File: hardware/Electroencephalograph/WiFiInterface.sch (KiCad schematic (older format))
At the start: 18 parts

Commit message: fix esp circuit
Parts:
- added R109, R110: 0R, Resistor_SMD:R_0402_1005Metric, symbol Device:R
- gave numbers to parts that had none: 18
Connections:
- net DP_GND: now also U12.9 (GND)
- net ESP_RX: now also R110.1; no longer J7.3 (Pin_3), U12.15 (RXD)
- net ESP_TX: now also R109.1; no longer J7.2 (Pin_2), U12.16 (TXD)
- net CS_ESP: now reaches U12.17 (CS0)
- net MISO: now reaches U12.18 (MISO)
- net MOSI: now reaches U12.21 (MOSI)
- net SCK: now reaches U12.22 (SCLK)
- net at U12.8 (VCC): now also C16.1, C17.1, Q2.3 (D), R103.1, R105.1, R106.1, R107.1
- new net: J7.3 (Pin_3), R110.2, U12.15 (RXD)
- new net: J7.2 (Pin_2), R109.2, U12.16 (TXD)
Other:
- moved on the sheet: D40, D41, J7, Q3, R102, R103, R104, R105, R106, R107, R108, U12

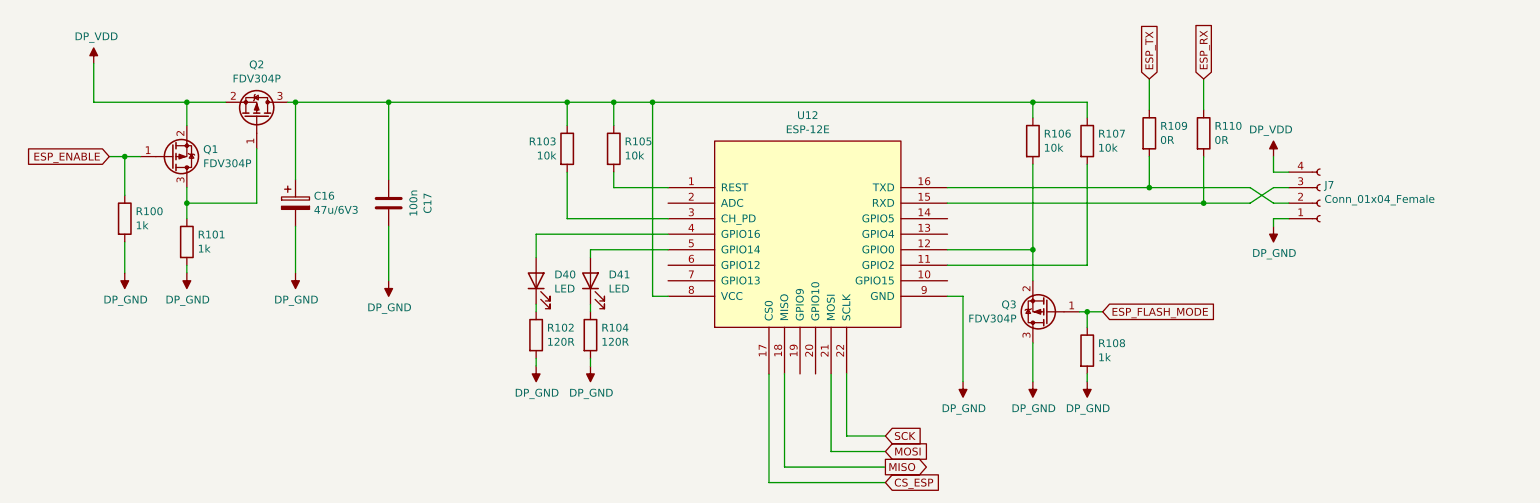
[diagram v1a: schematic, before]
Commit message: improve mcu component placement on pcb
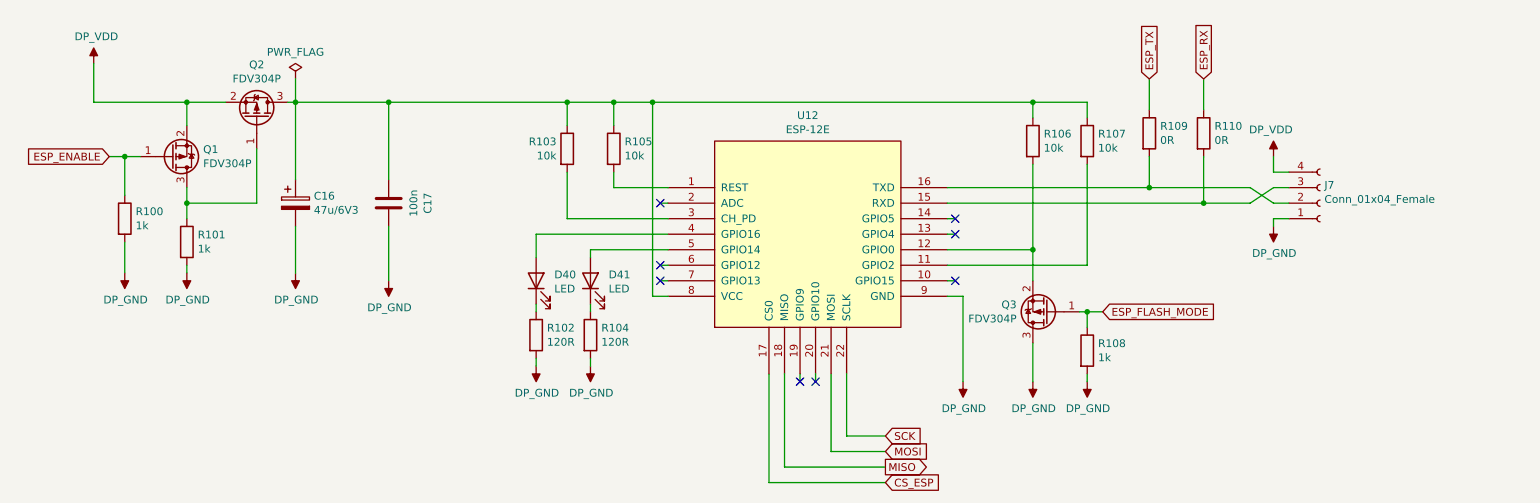
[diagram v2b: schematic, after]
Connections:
- no-connect marks 0 -> 8
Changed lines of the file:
@@
 Wire Wire Line
 	6200 5150 6200 4450
+Wire Wire Line
+	7350 3450 7400 3450
+Wire Wire Line
+	7350 3550 7400 3550
+Wire Wire Line
+	7350 3850 7400 3850
+NoConn ~ 7400 3450
+NoConn ~ 7400 3550
+NoConn ~ 7400 3850
+Wire Wire Line
+	5550 3350 5500 3350
+Wire Wire Line
+	5550 3750 5500 3750
+Wire Wire Line
+	5550 3850 5500 3850
+NoConn ~ 5500 3350
+NoConn ~ 5500 3750
+NoConn ~ 5500 3850
+Wire Wire Line
+	6400 4450 6400 4500
+Wire Wire Line
+	6500 4450 6500 4500
+NoConn ~ 6500 4500
+NoConn ~ 6400 4500
+$Comp
+L power:PWR_FLAG #FLG03
+U 1 1 5F0EAABE
+P 3150 2550
+F 0 "#FLG03" H 3150 2625 50  0001 C CNN
+F 1 "PWR_FLAG" H 3150 2723 50  0000 C CNN
+F 2 "" H 3150 2550 50  0001 C CNN
+F 3 "~" H 3150 2550 50  0001 C CNN
+	1    3150 2550
+	1    0    0    -1
+$EndComp
+Wire Wire Line
+	3150 2550 3150 2700
 $EndSCHEMATC

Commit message: draft of mcu routing
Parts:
- removed Q3: FDV304P, Package_TO_SOT_SMD:SOT-23, symbol Device:Q_PMOS_GSD
- removed R106: 10k, Resistor_SMD:R_0402_1005Metric, symbol Device:R
- added R116, R117: 0R, Resistor_SMD:R_0402_1005Metric, symbol Device:R
- R108: value 1k -> 10k
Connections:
- net DP_GND: no longer R108.2
- net ESP_FLASH_MODE: now also R108.2, U12.12 (GPIO0); no longer R108.1
- net at R110.2, U12.15 (RXD): now also R117.2; no longer J7.3 (Pin_3)
- net at R109.2, U12.16 (TXD): now also R116.2; no longer J7.2 (Pin_2)
- net at C16.1, C17.1, Q2.3 (D)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: now also R108.1
- new net: J7.2 (Pin_2), R116.1
- new net: J7.3 (Pin_3), R117.1
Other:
- moved on the sheet: C16, C17, Q1, Q2, R100, R101, R105, R107, R108, R109, R110

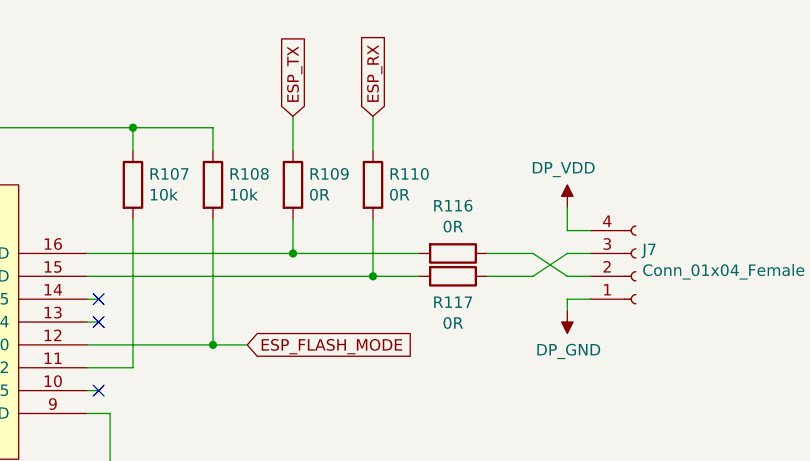
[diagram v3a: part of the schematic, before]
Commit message: further routing of cpu part
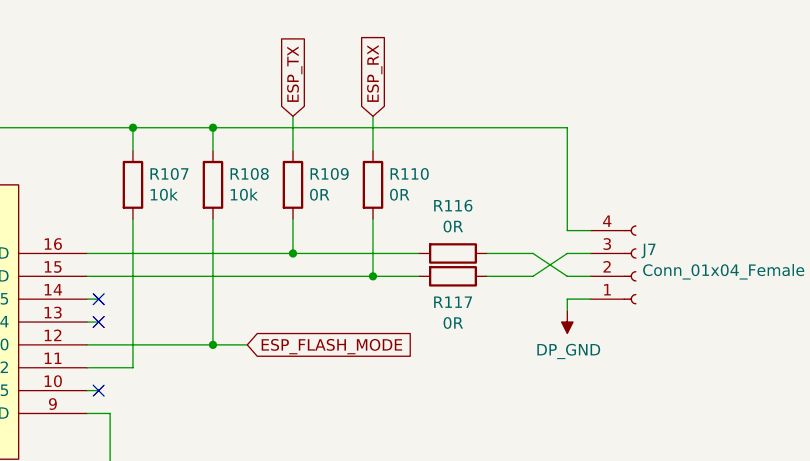
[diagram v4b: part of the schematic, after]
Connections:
- net DP_VDD: no longer J7.4 (Pin_4)
- net at C16.1, C17.1, Q2.3 (D)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: now also J7.4 (Pin_4)
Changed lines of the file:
@@
 	9550 3150 9450 3150
 Wire Wire Line
-	9450 3150 9450 3050
-Wire Wire Line
 	9450 3450 9450 3500
 Wire Wire Line
 	9550 3450 9450 3450
-$Comp
-L Electroencephalograph:DP_VDD #PWR?
-U 1 1 5F02CA0E
-P 9450 3050
-AR Path="/5E142744/5F02CA0E" Ref="#PWR?"  Part="1"
-AR Path="/5E27E78E/5F02CA0E" Ref="#PWR?"  Part="1"
-AR Path="/5F01FBEA/5F02CA0E" Ref="#PWR230"  Part="1"
-F 0 "#PWR230" H 9450 3175 50  0001 C CNN
-F 1 "DP_VDD" H 9467 3223 50  0000 C CNN
-F 2 "" H 9450 3175 50  0001 C CNN
-F 3 "" H 9450 3175 50  0001 C CNN
-	1    9450 3050
-	-1   0    0    -1
-$EndComp
 Wire Wire Line
 	4900 2700 4900 2850
@@
 Wire Wire Line
 	7900 3650 8050 3650
+Wire Wire Line
+	7900 2700 9450 2700
+Wire Wire Line
+	9450 2700 9450 3150
+Connection ~ 7900 2700
 $EndSCHEMATC

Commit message: further routing of mcu part
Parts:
- added C18: 100n, Capacitor_SMD:C_0402_1005Metric, symbol Device:C
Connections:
- net DP_GND: now also C18.2
- net at C16.1, C17.1, J7.4 (Pin_4)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: now also C18.1
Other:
- moved on the sheet: J7, R108, R109, R110, R116, R117
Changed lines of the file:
@@
 L Connector:Conn_01x04_Female J?
 U 1 1 5F02C9FE
-P 9750 3350
+P 10200 3350
 AR Path="/5E142744/5F02C9FE" Ref="J?"  Part="1"
 AR Path="/5E27E78E/5F02C9FE" Ref="J?"  Part="1"
 AR Path="/5F01FBEA/5F02C9FE" Ref="J7"  Part="1"
-F 0 "J7" H 9778 3234 50  0000 L CNN
-F 1 "Conn_01x04_Female" H 9778 3325 50  0000 L CNN
-F 2 "Connector_PinHeader_2.54mm:PinHeader_1x04_P2.54mm_Vertical" H 9750 3350 50  0001 C CNN
-F 3 "~" H 9750 3350 50  0001 C CNN
-	1    9750 3350
+F 0 "J7" H 10228 3234 50  0000 L CNN
+F 1 "Conn_01x04_Female" H 10228 3325 50  0000 L CNN
+F 2 "Connector_PinHeader_2.54mm:PinHeader_1x04_P2.54mm_Vertical" H 10200 3350 50  0001 C CNN
+F 3 "~" H 10200 3350 50  0001 C CNN
+	1    10200 3350
 	1    0    0    1
 $EndComp
@@
 L Electroencephalograph:DP_GND #PWR?
 U 1 1 5F02CA04
-P 9450 3500
+P 9900 3500
 AR Path="/5F02CA04" Ref="#PWR?"  Part="1"
 AR Path="/5DAEEEF4/5F02CA04" Ref="#PWR?"  Part="1"
@@
 AR Path="/5E27E78E/5F02CA04" Ref="#PWR?"  Part="1"
 AR Path="/5F01FBEA/5F02CA04" Ref="#PWR231"  Part="1"
-F 0 "#PWR231" H 9450 3250 50  0001 C CNN
-F 1 "DP_GND" H 9455 3327 50  0000 C CNN
-F 2 "" H 9450 3500 50  0001 C CNN
-F 3 "" H 9450 3500 50  0001 C CNN
-	1    9450 3500
-	1    0    0    -1
-$EndComp
-Wire Wire Line
-	9550 3150 9450 3150
-Wire Wire Line
-	9450 3450 9450 3500
-Wire Wire Line
-	9550 3450 9450 3450
+F 0 "#PWR231" H 9900 3250 50  0001 C CNN
+F 1 "DP_GND" H 9905 3327 50  0000 C CNN
+F 2 "" H 9900 3500 50  0001 C CNN
+F 3 "" H 9900 3500 50  0001 C CNN
+	1    9900 3500
+	1    0    0    -1
+$EndComp
+Wire Wire Line
+	10000 3150 9900 3150
+Wire Wire Line
+	9900 3450 9900 3500
+Wire Wire Line
+	10000 3450 9900 3450
 Wire Wire Line
 	4900 2700 4900 2850
@@
 L Device:R R?
 U 1 1 5F02CA80
-P 7900 2950
+P 8350 2950
 AR Path="/5DD5C7F6/5F02CA80" Ref="R?"  Part="1"
 AR Path="/5DD5CD1D/5F02CA80" Ref="R?"  Part="1"
 AR Path="/5E27E78E/5F02CA80" Ref="R?"  Part="1"
 AR Path="/5F01FBEA/5F02CA80" Ref="R108"  Part="1"
-F 0 "R108" H 7970 2996 50  0000 L CNN
-F 1 "10k" H 7970 2905 50  0000 L CNN
-F 2 "Resistor_SMD:R_0402_1005Metric" V 7830 2950 50  0001 C CNN
-F 3 "~" H 7900 2950 50  0001 C CNN
-	1    7900 2950
-	1    0    0    -1
-$EndComp
-Text GLabel 8050 3650 2    50   Input ~ 0
+F 0 "R108" H 8420 2996 50  0000 L CNN
+F 1 "10k" H 8420 2905 50  0000 L CNN
+F 2 "Resistor_SMD:R_0402_1005Metric" V 8280 2950 50  0001 C CNN
+F 3 "~" H 8350 2950 50  0001 C CNN
+	1    8350 2950
+	1    0    0    -1
+$EndComp
+Text GLabel 8500 3650 2    50   Input ~ 0
 ESP_FLASH_MODE
 Wire Wire Line
-	9300 3350 9450 3250
-Wire Wire Line
-	9450 3350 9300 3250
-Wire Wire Line
-	9450 3250 9550 3250
-Wire Wire Line
-	9450 3350 9550 3350
-Wire Wire Line
-	8600 3350 8600 3100
-Wire Wire Line
-	8600 3350 8800 3350
-Text GLabel 8250 2650 1    50   Input ~ 0
+	9750 3350 9900 3250
+Wire Wire Line
+	9900 3350 9750 3250
+Wire Wire Line
+	9900 3250 10000 3250
+Wire Wire Line
+	9900 3350 10000 3350
+Wire Wire Line
+	9050 3350 9050 3100
+Wire Wire Line
+	9050 3350 9250 3350
+Text GLabel 8700 2650 1    50   Input ~ 0
 ESP_TX
-Text GLabel 8600 2650 1    50   Input ~ 0
+Text GLabel 9050 2650 1    50   Input ~ 0
 ESP_RX
 Wire Wire Line
-	7350 3350 8600 3350
-Connection ~ 8600 3350
+	7350 3350 9050 3350
+Connection ~ 9050 3350
 $Comp
 L Device:LED D?
@@
 L Device:R R?
 U 1 1 5F04FD04
-P 8250 2950
+P 8700 2950
 AR Path="/5DD5C7F6/5F04FD04" Ref="R?"  Part="1"
 AR Path="/5DD5CD1D/5F04FD04" Ref="R?"  Part="1"
 AR Path="/5E27E78E/5F04FD04" Ref="R?"  Part="1"
 AR Path="/5F01FBEA/5F04FD04" Ref="R109"  Part="1"
-F 0 "R109" H 8320 2996 50  0000 L CNN
-F 1 "0R" H 8320 2905 50  0000 L CNN
-F 2 "Resistor_SMD:R_0402_1005Metric" V 8180 2950 50  0001 C CNN
-F 3 "~" H 8250 2950 50  0001 C CNN
-	1    8250 2950
-	1    0    0    -1
-$EndComp
-Wire Wire Line
-	7350 3250 8250 3250
-Wire Wire Line
-	8250 2800 8250 2650
-Wire Wire Line
-	8250 3100 8250 3250
-Connection ~ 8250 3250
-Wire Wire Line
-	8250 3250 8800 3250
+F 0 "R109" H 8770 2996 50  0000 L CNN
+F 1 "0R" H 8770 2905 50  0000 L CNN
+F 2 "Resistor_SMD:R_0402_1005Metric" V 8630 2950 50  0001 C CNN
+F 3 "~" H 8700 2950 50  0001 C CNN
+	1    8700 2950
+	1    0    0    -1
+$EndComp
+Wire Wire Line
+	7350 3250 8700 3250
+Wire Wire Line
+	8700 2800 8700 2650
+Wire Wire Line
+	8700 3100 8700 3250
+Connection ~ 8700 3250
+Wire Wire Line
+	8700 3250 9250 3250
 $Comp
 L Device:R R?
 U 1 1 5F054862
-P 8600 2950
+P 9050 2950
 AR Path="/5DD5C7F6/5F054862" Ref="R?"  Part="1"
 AR Path="/5DD5CD1D/5F054862" Ref="R?"  Part="1"
 AR Path="/5E27E78E/5F054862" Ref="R?"  Part="1"
 AR Path="/5F01FBEA/5F054862" Ref="R110"  Part="1"
-F 0 "R110" H 8670 2996 50  0000 L CNN
-F 1 "0R" H 8670 2905 50  0000 L CNN
-F 2 "Resistor_SMD:R_0402_1005Metric" V 8530 2950 50  0001 C CNN
-F 3 "~" H 8600 2950 50  0001 C CNN
-	1    8600 2950
-	1    0    0    -1
-$EndComp
-Wire Wire Line
-	8600 2800 8600 2650
+F 0 "R110" H 9120 2996 50  0000 L CNN
+F 1 "0R" H 9120 2905 50  0000 L CNN
+F 2 "Resistor_SMD:R_0402_1005Metric" V 8980 2950 50  0001 C CNN
+F 3 "~" H 9050 2950 50  0001 C CNN
+	1    9050 2950
+	1    0    0    -1
+$EndComp
+Wire Wire Line
+	9050 2800 9050 2650
 Text GLabel 6950 4850 2    50   Input ~ 0
 SCK
@@
 L Device:R R?
 U 1 1 5F160F1A
-P 8950 3250
+P 9400 3250
 AR Path="/5DD5C7F6/5F160F1A" Ref="R?"  Part="1"
 AR Path="/5DD5CD1D/5F160F1A" Ref="R?"  Part="1"
 AR Path="/5E27E78E/5F160F1A" Ref="R?"  Part="1"
 AR Path="/5F01FBEA/5F160F1A" Ref="R116"  Part="1"
-F 0 "R116" V 8743 3250 50  0000 C CNN
-F 1 "0R" V 8834 3250 50  0000 C CNN
-F 2 "Resistor_SMD:R_0402_1005Metric" V 8880 3250 50  0001 C CNN
-F 3 "~" H 8950 3250 50  0001 C CNN
-	1    8950 3250
+F 0 "R116" V 9193 3250 50  0000 C CNN
+F 1 "0R" V 9284 3250 50  0000 C CNN
+F 2 "Resistor_SMD:R_0402_1005Metric" V 9330 3250 50  0001 C CNN
+F 3 "~" H 9400 3250 50  0001 C CNN
+	1    9400 3250
 	0    1    1    0
 $EndComp
 Wire Wire Line
-	9100 3250 9300 3250
+	9550 3250 9750 3250
 $Comp
 L Device:R R?
 U 1 1 5F161272
-P 8950 3350
+P 9400 3350
 AR Path="/5DD5C7F6/5F161272" Ref="R?"  Part="1"
 AR Path="/5DD5CD1D/5F161272" Ref="R?"  Part="1"
 AR Path="/5E27E78E/5F161272" Ref="R?"  Part="1"
 AR Path="/5F01FBEA/5F161272" Ref="R117"  Part="1"
-F 0 "R117" V 9065 3350 50  0000 C CNN
-F 1 "0R" V 9156 3350 50  0000 C CNN
-F 2 "Resistor_SMD:R_0402_1005Metric" V 8880 3350 50  0001 C CNN
-F 3 "~" H 8950 3350 50  0001 C CNN
-	1    8950 3350
+F 0 "R117" V 9515 3350 50  0000 C CNN
+F 1 "0R" V 9606 3350 50  0000 C CNN
+F 2 "Resistor_SMD:R_0402_1005Metric" V 9330 3350 50  0001 C CNN
+F 3 "~" H 9400 3350 50  0001 C CNN
+	1    9400 3350
 	0    1    1    0
 $EndComp
 Wire Wire Line
-	9100 3350 9300 3350
+	9550 3350 9750 3350
 Wire Wire Line
 	5450 2700 7550 2700
 Wire Wire Line
-	7550 2700 7900 2700
-Wire Wire Line
-	7900 2700 7900 2800
+	7550 2700 7950 2700
+Wire Wire Line
+	8350 2700 8350 2800
 Connection ~ 7550 2700
 Wire Wire Line
-	7900 3100 7900 3650
-Wire Wire Line
-	7350 3650 7900 3650
-Connection ~ 7900 3650
-Wire Wire Line
-	7900 3650 8050 3650
-Wire Wire Line
-	7900 2700 9450 2700
-Wire Wire Line
-	9450 2700 9450 3150
-Connection ~ 7900 2700
+	8350 3100 8350 3650
+Wire Wire Line
+	7350 3650 8350 3650
+Connection ~ 8350 3650
+Wire Wire Line
+	8350 3650 8500 3650
+Wire Wire Line
+	8350 2700 9900 2700
+Wire Wire Line
+	9900 2700 9900 3150
+Connection ~ 8350 2700
+$Comp
+L Device:C C?
+U 1 1 5F0FAD1C
+P 7950 2950
+AR Path="/5F0FAD1C" Ref="C?"  Part="1"
+AR Path="/5DAEEEF4/5F0FAD1C" Ref="C?"  Part="1"
+AR Path="/5DD5C7F6/5F0FAD1C" Ref="C?"  Part="1"
+AR Path="/5DD5CD1D/5F0FAD1C" Ref="C?"  Part="1"
+AR Path="/5E27E78E/5F0FAD1C" Ref="C?"  Part="1"
+AR Path="/5F01FBEA/5F0FAD1C" Ref="C18"  Part="1"
+F 0 "C18" H 8065 2996 50  0000 L CNN
+F 1 "100n" H 8065 2905 50  0000 L CNN
+F 2 "Capacitor_SMD:C_0402_1005Metric" H 7988 2800 50  0001 C CNN
+F 3 "~" H 7950 2950 50  0001 C CNN
+	1    7950 2950
+	1    0    0    -1
+$EndComp
+$Comp
+L Electroencephalograph:DP_GND #PWR?
+U 1 1 5F0FB11C
+P 7950 4500
+AR Path="/5F0FB11C" Ref="#PWR?"  Part="1"
+AR Path="/5DAEEEF4/5F0FB11C" Ref="#PWR?"  Part="1"
+AR Path="/5DD5C7F6/5F0FB11C" Ref="#PWR?"  Part="1"
+AR Path="/5DD5CD1D/5F0FB11C" Ref="#PWR?"  Part="1"
+AR Path="/5E27E78E/5F0FB11C" Ref="#PWR?"  Part="1"
+AR Path="/5F01FBEA/5F0FB11C" Ref="#PWR228"  Part="1"
+F 0 "#PWR228" H 7950 4250 50  0001 C CNN
+F 1 "DP_GND" H 7955 4327 50  0000 C CNN
+F 2 "" H 7950 4500 50  0001 C CNN
+F 3 "" H 7950 4500 50  0001 C CNN
+	1    7950 4500
+	1    0    0    -1
+$EndComp
+Wire Wire Line
+	7950 4500 7950 3100
+Wire Wire Line
+	7950 2800 7950 2700
+Connection ~ 7950 2700
+Wire Wire Line
+	7950 2700 8350 2700
 $EndSCHEMATC
